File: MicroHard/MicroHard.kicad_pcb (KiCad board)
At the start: 4 copper layers, 0 parts

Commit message: Initial layout
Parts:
- added C1: 100n, Capacitor_SMD:C_1206_3216Metric_Pad1.33x1.80mm_HandSolder, F.Cu at (233.0, 79.0)
- added C10: 100n, Capacitor_SMD:C_1206_3216Metric_Pad1.33x1.80mm_HandSolder, F.Cu at (233.0, 85.5)
- added C11: 10u, Capacitor_SMD:C_1206_3216Metric_Pad1.33x1.80mm_HandSolder, F.Cu at (217.1, 80.0)
- added C12: 100n, Capacitor_SMD:C_1206_3216Metric_Pad1.33x1.80mm_HandSolder, F.Cu at (216.9, 85.5)
- added C13: 100n, Capacitor_SMD:C_1206_3216Metric_Pad1.33x1.80mm_HandSolder, F.Cu at (216.9, 90.5)
- added C14: 100n, Capacitor_SMD:C_1206_3216Metric_Pad1.33x1.80mm_HandSolder, F.Cu at (233.0, 90.5)
- added C15: 22u, Capacitor_SMD:C_1206_3216Metric_Pad1.33x1.80mm_HandSolder, F.Cu at (204.0, 84.6)
- added C16: 22u, Capacitor_SMD:C_1206_3216Metric_Pad1.33x1.80mm_HandSolder, F.Cu at (199.0, 84.5)
- added C17: 22u, Capacitor_SMD:C_1206_3216Metric_Pad1.33x1.80mm_HandSolder, F.Cu at (204.0, 91.0)
- added C18: 22u, Capacitor_SMD:C_1206_3216Metric_Pad1.33x1.80mm_HandSolder, F.Cu at (199.0, 91.0)
- added C19: 1u, Capacitor_SMD:C_1206_3216Metric_Pad1.33x1.80mm_HandSolder, F.Cu at (225.4, 94.2)
- added C2: 100u, Capacitor_SMD:C_1210_3225Metric_Pad1.33x2.70mm_HandSolder, F.Cu at (225.2, 66.5)
- added C20: 30p, Capacitor_SMD:C_0805_2012Metric_Pad1.18x1.45mm_HandSolder, F.Cu at (186.0, 136.8)
- added C21: 30p, Capacitor_SMD:C_0805_2012Metric_Pad1.18x1.45mm_HandSolder, F.Cu at (186.0, 133.8)
- added C22: 10u, Capacitor_SMD:C_1206_3216Metric_Pad1.33x1.80mm_HandSolder, F.Cu at (175.4, 121.7)
- added C23: 10n, Capacitor_SMD:C_1206_3216Metric_Pad1.33x1.80mm_HandSolder, F.Cu at (175.4, 118.3)
- added C24: 10n, Capacitor_SMD:C_1206_3216Metric_Pad1.33x1.80mm_HandSolder, F.Cu at (175.4, 115.0)
- added C25: 1u, Capacitor_SMD:C_1206_3216Metric_Pad1.33x1.80mm_HandSolder, F.Cu at (175.4, 111.7)
- added C26: 10u, Capacitor_SMD:C_1206_3216Metric_Pad1.33x1.80mm_HandSolder, F.Cu at (175.4, 108.3)
- added C27: 100n, Capacitor_SMD:C_1206_3216Metric_Pad1.33x1.80mm_HandSolder, F.Cu at (202.6, 108.3)
- added C28: 10u, Capacitor_SMD:C_1206_3216Metric_Pad1.33x1.80mm_HandSolder, F.Cu at (202.6, 112.3)
- added C29: 100n, Capacitor_SMD:C_1206_3216Metric_Pad1.33x1.80mm_HandSolder, F.Cu at (202.6, 115.7)
- added C3: 10u, Capacitor_SMD:C_1206_3216Metric_Pad1.33x1.80mm_HandSolder, F.Cu at (233.0, 71.2)
- added C30: 100n, Capacitor_SMD:C_1206_3216Metric_Pad1.33x1.80mm_HandSolder, F.Cu at (202.6, 119.0)
- added C31: 100n, Capacitor_SMD:C_1206_3216Metric_Pad1.33x1.80mm_HandSolder, F.Cu at (202.6, 122.3)
- added C32: 100u, Capacitor_SMD:C_1210_3225Metric_Pad1.33x2.70mm_HandSolder, F.Cu at (85.3, 141.9)
- added C33: 4.7u, Capacitor_SMD:C_0805_2012Metric_Pad1.18x1.45mm_HandSolder, F.Cu at (79.9, 141.3)
- added C34: 4.7u, Capacitor_SMD:C_0805_2012Metric_Pad1.18x1.45mm_HandSolder, F.Cu at (79.9, 144.3)
- added C35: 470n, Capacitor_SMD:C_0603_1608Metric_Pad1.08x0.95mm_HandSolder, F.Cu at (124.0, 129.8)
- added C36: 470n, Capacitor_SMD:C_0603_1608Metric_Pad1.08x0.95mm_HandSolder, F.Cu at (124.0, 132.3)
- added C37: 470n, Capacitor_SMD:C_0603_1608Metric_Pad1.08x0.95mm_HandSolder, F.Cu at (124.0, 134.8)
- added C38: 470n, Capacitor_SMD:C_0603_1608Metric_Pad1.08x0.95mm_HandSolder, F.Cu at (124.0, 137.3)
- added C39: 470n, Capacitor_SMD:C_0603_1608Metric_Pad1.08x0.95mm_HandSolder, F.Cu at (124.0, 139.8)
- added C4: 100n, Capacitor_SMD:C_1206_3216Metric_Pad1.33x1.80mm_HandSolder, F.Cu at (233.0, 75.0)
- added C40: 470n, Capacitor_SMD:C_0603_1608Metric_Pad1.08x0.95mm_HandSolder, F.Cu at (124.0, 142.3)
- added C41: 4.7u, Capacitor_SMD:C_0805_2012Metric_Pad1.18x1.45mm_HandSolder, F.Cu at (79.9, 147.3)
- added C42: 100u, Capacitor_SMD:C_1210_3225Metric_Pad1.33x2.70mm_HandSolder, F.Cu at (85.3, 146.2)
- added C43: 470n, Capacitor_SMD:C_0603_1608Metric_Pad1.08x0.95mm_HandSolder, F.Cu at (124.0, 144.8)
- added C44: 470n, Capacitor_SMD:C_0603_1608Metric_Pad1.08x0.95mm_HandSolder, F.Cu at (124.0, 147.3)
- added C45: 4.7u, Capacitor_SMD:C_0805_2012Metric_Pad1.18x1.45mm_HandSolder, F.Cu at (79.9, 150.3)
- added C46: 10n, Capacitor_SMD:C_1206_3216Metric_Pad1.33x1.80mm_HandSolder, F.Cu at (85.3, 150.0)
- added C47: 47u, Capacitor_SMD:C_1210_3225Metric_Pad1.33x2.70mm_HandSolder, F.Cu at (110.0, 155.8)
- added C48: 330u, Capacitor_Tantalum_SMD:CP_EIA-7343-31_Kemet-D_Pad2.25x2.55mm_HandSolder, F.Cu at (134.5, 145.3)
- added C49: 4.7u, Capacitor_SMD:C_0805_2012Metric_Pad1.18x1.45mm_HandSolder, F.Cu at (116.5, 147.3)
- added C5: 22u, Capacitor_SMD:C_1206_3216Metric_Pad1.33x1.80mm_HandSolder, F.Cu at (204.0, 78.9)
- added C50: 4.7u, Capacitor_SMD:C_0805_2012Metric_Pad1.18x1.45mm_HandSolder, F.Cu at (113.5, 147.3)
- added C51: 4.7u, Capacitor_SMD:C_0805_2012Metric_Pad1.18x1.45mm_HandSolder, F.Cu at (110.5, 147.3)
- added C52: 4.7u, Capacitor_SMD:C_0805_2012Metric_Pad1.18x1.45mm_HandSolder, F.Cu at (107.5, 147.3)
- added C53: 4.7u, Capacitor_SMD:C_0805_2012Metric_Pad1.18x1.45mm_HandSolder, F.Cu at (104.5, 147.3)
- added C54: 4.7u, Capacitor_SMD:C_0805_2012Metric_Pad1.18x1.45mm_HandSolder, F.Cu at (101.4, 147.3)
- added C55: 470n, Capacitor_SMD:C_0603_1608Metric_Pad1.08x0.95mm_HandSolder, F.Cu at (96.6, 139.6)
- added C56: 470n, Capacitor_SMD:C_0603_1608Metric_Pad1.08x0.95mm_HandSolder, F.Cu at (96.6, 137.1)
- added C57: 470n, Capacitor_SMD:C_0603_1608Metric_Pad1.08x0.95mm_HandSolder, F.Cu at (96.6, 134.5)
- added C58: 470n, Capacitor_SMD:C_0603_1608Metric_Pad1.08x0.95mm_HandSolder, F.Cu at (96.6, 132.0)
- added C59: 470n, Capacitor_SMD:C_0603_1608Metric_Pad1.08x0.95mm_HandSolder, F.Cu at (96.6, 129.5)
- added C6: 22u, Capacitor_SMD:C_1206_3216Metric_Pad1.33x1.80mm_HandSolder, F.Cu at (199.0, 79.0)
- added C60: 470n, Capacitor_SMD:C_0603_1608Metric_Pad1.08x0.95mm_HandSolder, F.Cu at (98.5, 121.2)
- added C61: 470n, Capacitor_SMD:C_0603_1608Metric_Pad1.08x0.95mm_HandSolder, F.Cu at (101.0, 121.2)
- added C62: 470n, Capacitor_SMD:C_0603_1608Metric_Pad1.08x0.95mm_HandSolder, F.Cu at (103.5, 121.2)
- added C63: 47u, Capacitor_SMD:C_1210_3225Metric_Pad1.33x2.70mm_HandSolder, F.Cu at (91.0, 121.3)
- added C64: 4.7u, Capacitor_SMD:C_0805_2012Metric_Pad1.18x1.45mm_HandSolder, F.Cu at (98.4, 147.3)
- added C65: 4.7u, Capacitor_SMD:C_0805_2012Metric_Pad1.18x1.45mm_HandSolder, F.Cu at (95.4, 147.3)
- added C66: 470n, Capacitor_SMD:C_0603_1608Metric_Pad1.08x0.95mm_HandSolder, F.Cu at (106.0, 121.2)
- added C67: 470n, Capacitor_SMD:C_0603_1608Metric_Pad1.08x0.95mm_HandSolder, F.Cu at (108.5, 121.2)
- added C68: 470n, Capacitor_SMD:C_0603_1608Metric_Pad1.08x0.95mm_HandSolder, F.Cu at (111.0, 121.3)
- added C69: 100u, Capacitor_SMD:C_1210_3225Metric_Pad1.33x2.70mm_HandSolder, F.Cu at (124.0, 121.8)
- added C7: 3.3n, Capacitor_SMD:C_1206_3216Metric_Pad1.33x1.80mm_HandSolder, F.Cu at (217.1, 75.5)
- added C70: 470n, Capacitor_SMD:C_0603_1608Metric_Pad1.08x0.95mm_HandSolder, F.Cu at (113.5, 121.3)
- added C71: 470n, Capacitor_SMD:C_0603_1608Metric_Pad1.08x0.95mm_HandSolder, F.Cu at (116.0, 121.3)
- added C72: 47u, Capacitor_SMD:C_1210_3225Metric_Pad1.33x2.70mm_HandSolder, F.Cu at (180.7, 86.3)
- added C73: 100n, Capacitor_SMD:C_1206_3216Metric_Pad1.33x1.80mm_HandSolder, F.Cu at (180.7, 89.8)
- added C74: 11p, Capacitor_SMD:C_0805_2012Metric_Pad1.18x1.45mm_HandSolder, F.Cu at (180.2, 92.8)
- added C75: 1u, Capacitor_SMD:C_1206_3216Metric_Pad1.33x1.80mm_HandSolder, F.Cu at (70.0, 98.8)
- added C76: 100n, Capacitor_SMD:C_1206_3216Metric_Pad1.33x1.80mm_HandSolder, F.Cu at (70.0, 95.5)
- added C77: 1u, Capacitor_SMD:C_1206_3216Metric_Pad1.33x1.80mm_HandSolder, F.Cu at (90.1, 99.4)
- added C78: 100n, Capacitor_SMD:C_1206_3216Metric_Pad1.33x1.80mm_HandSolder, F.Cu at (90.1, 96.0)
- added C79: 4p, Capacitor_SMD:C_1206_3216Metric_Pad1.33x1.80mm_HandSolder, F.Cu at (93.5, 59.8)
- added C8: 1u, Capacitor_SMD:C_1206_3216Metric_Pad1.33x1.80mm_HandSolder, F.Cu at (217.1, 71.0)
- added C80: 100n, Capacitor_SMD:C_1206_3216Metric_Pad1.33x1.80mm_HandSolder, F.Cu at (139.5, 110.3)
- added C81: 100n, Capacitor_SMD:C_1206_3216Metric_Pad1.33x1.80mm_HandSolder, F.Cu at (122.0, 100.3)
- added C9: 10u, Capacitor_SMD:C_1206_3216Metric_Pad1.33x1.80mm_HandSolder, F.Cu at (225.0, 80.0)
- added D1: LED, LED_SMD:LED_1206_3216Metric_Pad1.42x1.75mm_HandSolder, F.Cu at (216.9, 61.5)
- added D2: LED, LED_SMD:LED_1206_3216Metric_Pad1.42x1.75mm_HandSolder, F.Cu at (213.9, 116.6)
- added D3: LED, LED_SMD:LED_1206_3216Metric_Pad1.42x1.75mm_HandSolder, F.Cu at (219.4, 116.6)
- added D4: LED, LED_SMD:LED_1206_3216Metric_Pad1.42x1.75mm_HandSolder, F.Cu at (77.4, 132.2)
- added D5: LED, LED_SMD:LED_1206_3216Metric_Pad1.42x1.75mm_HandSolder, F.Cu at (77.4, 128.8)
- added D6: LED, LED_SMD:LED_1206_3216Metric_Pad1.42x1.75mm_HandSolder, F.Cu at (77.4, 125.4)
- added D7: LED, LED_SMD:LED_1206_3216Metric_Pad1.42x1.75mm_HandSolder, F.Cu at (77.4, 122.0)
- added FB1: FerriteBead, Resistor_SMD:R_1206_3216Metric_Pad1.30x1.75mm_HandSolder, F.Cu at (176.5, 136.0)
- added IC1: IS66WVO32M8DBLL-166BLI, MicroHard:BGA24C100P5X5_600X800X120, F.Cu at (113.0, 97.8)
- added J1: USB_B_Micro, Connector_USB:USB_Micro-B_Amphenol_10118194_Horizontal, F.Cu at (233.7, 62.5)
- added J2: Micro_SD_Card_Det2, Connector_Card:microSD_HC_Hirose_DM3AT-SF-PEJM5, F.Cu at (240.0, 114.8)
- added J3: GPIO_header, Connector_PinHeader_2.54mm:PinHeader_1x08_P2.54mm_Vertical, F.Cu at (166.5, 128.2)
- added J4: MCU_Debug, Connector_PinHeader_1.00mm:PinHeader_2x10_P1.00mm_Vertical, F.Cu at (207.9, 146.3)
- added J5: Controller Connector, Connector_PinHeader_2.54mm:PinHeader_1x07_P2.54mm_Vertical, F.Cu at (177.3, 146.8)
- added J6: FPGA_GPIO_header, Connector_JST:JST_XH_B8B-XH-AM_1x08_P2.50mm_Vertical, F.Cu at (161.0, 128.4)
- added J7: FPGA_DEBUG, MicroHard:MOLEX_87832-1420, F.Cu at (67.8, 126.3)
- added J8: L77HDE15SD1CH4FVGA, MicroHard:AMPHENOL_L77HDE15SD1CH4FVGA, F.Cu at (73.4, 57.9)
- added JP1: Jumper_2_Bridged, Connector_PinHeader_2.54mm:PinHeader_1x02_P2.54mm_Vertical, F.Cu at (191.8, 79.3)
- added JP2: Jumper_2_Bridged, Connector_PinHeader_2.54mm:PinHeader_1x02_P2.54mm_Vertical, F.Cu at (191.8, 84.0)
- added JP3: Jumper_2_Bridged, Connector_PinHeader_2.54mm:PinHeader_1x02_P2.54mm_Vertical, F.Cu at (191.8, 88.7)
- added L1: 1.5u, Inductor_SMD:L_1206_3216Metric_Pad1.42x1.75mm_HandSolder, F.Cu at (209.7, 79.0)
- added L2: 1.5u, Inductor_SMD:L_1206_3216Metric_Pad1.42x1.75mm_HandSolder, F.Cu at (209.7, 85.0)
- added L3: 2.2u, Inductor_SMD:L_1206_3216Metric_Pad1.42x1.75mm_HandSolder, F.Cu at (210.2, 91.0)
- added LED1: LTP-587HR, LTP-587HR:LTP-587HR_LTO, F.Cu at (103.1, 52.2)
- added LED2: LTP-587HR, LTP-587HR:LTP-587HR_LTO, F.Cu at (120.8, 52.2)
- added LED3: LTP-587HR, LTP-587HR:LTP-587HR_LTO, F.Cu at (138.5, 52.2)
- added LED4: LTP-587HR, LTP-587HR:LTP-587HR_LTO, F.Cu at (156.1, 52.2)
- added LED5: LTP-587HR, LTP-587HR:LTP-587HR_LTO, F.Cu at (173.8, 52.2)
- added LED6: LTP-587HR, LTP-587HR:LTP-587HR_LTO, F.Cu at (191.4, 52.2)
- added R1: 6.81k, Resistor_SMD:R_1206_3216Metric_Pad1.30x1.75mm_HandSolder, B.Cu at (210.3, 69.5)
- added R10: 22.1k, Resistor_SMD:R_1206_3216Metric_Pad1.30x1.75mm_HandSolder, B.Cu at (205.1, 86.0)
- added R11: 68, Resistor_SMD:R_1206_3216Metric_Pad1.30x1.75mm_HandSolder, F.Cu at (213.9, 110.6)
- added R12: 10k, Resistor_SMD:R_1206_3216Metric_Pad1.30x1.75mm_HandSolder, F.Cu at (221.5, 125.8)
- added R13: 68, Resistor_SMD:R_1206_3216Metric_Pad1.30x1.75mm_HandSolder, F.Cu at (219.4, 110.6)
- added R14: 10k, Resistor_SMD:R_1206_3216Metric_Pad1.30x1.75mm_HandSolder, F.Cu at (213.0, 125.8)
- added R15: 10k, Resistor_SMD:R_1206_3216Metric_Pad1.30x1.75mm_HandSolder, F.Cu at (140.0, 83.8)
- added R16: 200, Resistor_SMD:R_1206_3216Metric_Pad1.30x1.75mm_HandSolder, F.Cu at (68.5, 140.6)
- added R17: 4.7k, Resistor_SMD:R_1206_3216Metric_Pad1.30x1.75mm_HandSolder, F.Cu at (68.5, 143.8)
- added R18: 10k, Resistor_SMD:R_1206_3216Metric_Pad1.30x1.75mm_HandSolder, F.Cu at (68.5, 147.1)
- added R19: 10k, Resistor_SMD:R_1206_3216Metric_Pad1.30x1.75mm_HandSolder, F.Cu at (68.5, 150.4)
- added R2: 100k, Resistor_SMD:R_1206_3216Metric_Pad1.30x1.75mm_HandSolder, B.Cu at (210.2, 74.9)
- added R20: 4.7k, Resistor_SMD:R_1206_3216Metric_Pad1.30x1.75mm_HandSolder, F.Cu at (132.5, 83.9)
- added R21: 100, Resistor_SMD:R_1206_3216Metric_Pad1.30x1.75mm_HandSolder, F.Cu at (83.4, 132.1)
- added R22: 330, Resistor_SMD:R_1206_3216Metric_Pad1.30x1.75mm_HandSolder, F.Cu at (83.4, 128.8)
- added R23: 330, Resistor_SMD:R_1206_3216Metric_Pad1.30x1.75mm_HandSolder, F.Cu at (83.4, 125.5)
- added R24: 330, Resistor_SMD:R_1206_3216Metric_Pad1.30x1.75mm_HandSolder, F.Cu at (83.4, 122.3)
- added R25: 4.7k, Resistor_SMD:R_1206_3216Metric_Pad1.30x1.75mm_HandSolder, F.Cu at (154.2, 85.8)
- added R26: 4.7k, Resistor_SMD:R_1206_3216Metric_Pad1.30x1.75mm_HandSolder, F.Cu at (154.2, 88.8)
- added R27: 112k, Resistor_SMD:R_1206_3216Metric_Pad1.30x1.75mm_HandSolder, F.Cu at (154.2, 92.3)
- added R28: 100k, Resistor_SMD:R_1206_3216Metric_Pad1.30x1.75mm_HandSolder, B.Cu at (69.4, 109.8)
- added R29: 100k, Resistor_SMD:R_1206_3216Metric_Pad1.30x1.75mm_HandSolder, B.Cu at (72.7, 109.8)
- added R3: 22.1k, Resistor_SMD:R_1206_3216Metric_Pad1.30x1.75mm_HandSolder, B.Cu at (210.4, 65.0)
- added R30: 100k, Resistor_SMD:R_1206_3216Metric_Pad1.30x1.75mm_HandSolder, B.Cu at (76.0, 109.8)
- added R31: 100k, Resistor_SMD:R_1206_3216Metric_Pad1.30x1.75mm_HandSolder, B.Cu at (79.3, 109.8)
- added R32: 536, Resistor_SMD:R_1206_3216Metric_Pad1.30x1.75mm_HandSolder, F.Cu at (62.0, 73.4)
- added R33: 270, Resistor_SMD:R_1206_3216Metric_Pad1.30x1.75mm_HandSolder, F.Cu at (65.0, 70.4)
- added R34: 536, Resistor_SMD:R_1206_3216Metric_Pad1.30x1.75mm_HandSolder, F.Cu at (68.0, 73.4)
- added R35: 536, Resistor_SMD:R_1206_3216Metric_Pad1.30x1.75mm_HandSolder, F.Cu at (91.0, 85.3)
- added R36: 100k, Resistor_SMD:R_1206_3216Metric_Pad1.30x1.75mm_HandSolder, B.Cu at (92.1, 109.8)
- added R37: 100k, Resistor_SMD:R_1206_3216Metric_Pad1.30x1.75mm_HandSolder, B.Cu at (88.8, 109.8)
- added R38: 100k, Resistor_SMD:R_1206_3216Metric_Pad1.30x1.75mm_HandSolder, B.Cu at (85.5, 109.8)
- added R39: 100k, Resistor_SMD:R_1206_3216Metric_Pad1.30x1.75mm_HandSolder, B.Cu at (82.2, 109.8)
- added R4: 1, Resistor_SMD:R_1206_3216Metric_Pad1.30x1.75mm_HandSolder, F.Cu at (176.4, 140.5)
- added R40: 270, Resistor_SMD:R_1206_3216Metric_Pad1.30x1.75mm_HandSolder, F.Cu at (71.0, 70.4)
- added R41: 270, Resistor_SMD:R_1206_3216Metric_Pad1.30x1.75mm_HandSolder, F.Cu at (94.5, 82.3)
- added R42: 536, Resistor_SMD:R_1206_3216Metric_Pad1.30x1.75mm_HandSolder, F.Cu at (74.0, 73.4)
- added R43: 536, Resistor_SMD:R_1206_3216Metric_Pad1.30x1.75mm_HandSolder, F.Cu at (98.0, 85.3)
- added R44: 536, Resistor_SMD:R_1206_3216Metric_Pad1.30x1.75mm_HandSolder, F.Cu at (63.9, 85.3)
- added R45: 270, Resistor_SMD:R_1206_3216Metric_Pad1.30x1.75mm_HandSolder, F.Cu at (77.0, 70.4)
- added R46: 270, Resistor_SMD:R_1206_3216Metric_Pad1.30x1.75mm_HandSolder, F.Cu at (101.5, 82.3)
- added R47: 270, Resistor_SMD:R_1206_3216Metric_Pad1.30x1.75mm_HandSolder, F.Cu at (67.0, 81.3)
- added R48: 536, Resistor_SMD:R_1206_3216Metric_Pad1.30x1.75mm_HandSolder, F.Cu at (80.5, 73.4)
- added R49: 536, Resistor_SMD:R_1206_3216Metric_Pad1.30x1.75mm_HandSolder, F.Cu at (104.5, 85.3)
- added R5: 30.1k, Resistor_SMD:R_1206_3216Metric_Pad1.30x1.75mm_HandSolder, B.Cu at (198.6, 81.5)
- added R50: 536, Resistor_SMD:R_1206_3216Metric_Pad1.30x1.75mm_HandSolder, F.Cu at (70.5, 85.3)
- added R51: 536, Resistor_SMD:R_1206_3216Metric_Pad1.30x1.75mm_HandSolder, F.Cu at (83.5, 70.4)
- added R52: 270, Resistor_SMD:R_1206_3216Metric_Pad1.30x1.75mm_HandSolder, F.Cu at (107.5, 82.3)
- added R53: 270, Resistor_SMD:R_1206_3216Metric_Pad1.30x1.75mm_HandSolder, F.Cu at (74.0, 81.8)
- added R54: 536, Resistor_SMD:R_1206_3216Metric_Pad1.30x1.75mm_HandSolder, F.Cu at (110.5, 85.8)
- added R55: 536, Resistor_SMD:R_1206_3216Metric_Pad1.30x1.75mm_HandSolder, F.Cu at (77.5, 85.3)
- added R56: 536, Resistor_SMD:R_1206_3216Metric_Pad1.30x1.75mm_HandSolder, F.Cu at (113.5, 82.3)
- added R57: 270, Resistor_SMD:R_1206_3216Metric_Pad1.30x1.75mm_HandSolder, F.Cu at (81.0, 81.8)
- added R58: 536, Resistor_SMD:R_1206_3216Metric_Pad1.30x1.75mm_HandSolder, F.Cu at (84.5, 85.3)
- added R59: 1MEG, Resistor_SMD:R_1206_3216Metric_Pad1.30x1.75mm_HandSolder, F.Cu at (93.4, 63.8)
- added R6: 73.2k, Resistor_SMD:R_1206_3216Metric_Pad1.30x1.75mm_HandSolder, B.Cu at (198.6, 86.0)
- added R60: 536, Resistor_SMD:R_1206_3216Metric_Pad1.30x1.75mm_HandSolder, F.Cu at (87.5, 81.8)
- added R61: 100k, Resistor_SMD:R_1206_3216Metric_Pad1.30x1.75mm_HandSolder, B.Cu at (96.8, 109.8)
- added R62: 100k, Resistor_SMD:R_1206_3216Metric_Pad1.30x1.75mm_HandSolder, B.Cu at (100.1, 109.8)
- added R63: 100k, Resistor_SMD:R_1206_3216Metric_Pad1.30x1.75mm_HandSolder, B.Cu at (104.5, 109.8)
- added R64: 100k, Resistor_SMD:R_1206_3216Metric_Pad1.30x1.75mm_HandSolder, B.Cu at (107.8, 109.8)
- added R65: 100, Resistor_SMD:R_1206_3216Metric_Pad1.30x1.75mm_HandSolder, F.Cu at (93.4, 68.8)
- added R66: 100, Resistor_SMD:R_1206_3216Metric_Pad1.30x1.75mm_HandSolder, F.Cu at (93.4, 72.1)
- added R67: 100k, Resistor_SMD:R_1206_3216Metric_Pad1.30x1.75mm_HandSolder, B.Cu at (114.5, 109.8)
- added R68: 100k, Resistor_SMD:R_1206_3216Metric_Pad1.30x1.75mm_HandSolder, B.Cu at (111.0, 109.8)
- added R69: 4.7k, Resistor_SMD:R_1206_3216Metric_Pad1.30x1.75mm_HandSolder, B.Cu at (139.4, 106.3)
- added R7: 100k, Resistor_SMD:R_1206_3216Metric_Pad1.30x1.75mm_HandSolder, B.Cu at (225.0, 94.2)
- added R70: 2.4k, Resistor_SMD:R_1206_3216Metric_Pad1.30x1.75mm_HandSolder, B.Cu at (141.9, 119.3)
- added R71: 4.7k, Resistor_SMD:R_1206_3216Metric_Pad1.30x1.75mm_HandSolder, F.Cu at (160.5, 111.3)
- added R72: 2.4k, Resistor_SMD:R_1206_3216Metric_Pad1.30x1.75mm_HandSolder, F.Cu at (122.0, 93.5)
- added R73: 2.4k, Resistor_SMD:R_1206_3216Metric_Pad1.30x1.75mm_HandSolder, F.Cu at (122.0, 96.8)
- added R8: 68, Resistor_SMD:R_1206_3216Metric_Pad1.30x1.75mm_HandSolder, F.Cu at (216.9, 66.5)
- added R9: 22.1k, Resistor_SMD:R_1206_3216Metric_Pad1.30x1.75mm_HandSolder, B.Cu at (205.1, 81.5)
- added SW1: KMR221NGLFS, KMR221NG:KMR221_CNK, F.Cu at (221.6, 132.1)
- added SW2: KMR221NGLFS, KMR221NG:KMR221_CNK, F.Cu at (212.9, 132.1)
- added SW3: KMR221NGLFS, KMR221NG:KMR221_CNK, F.Cu at (140.0, 91.8)
- added SW4: KMR221NGLFS, KMR221NG:KMR221_CNK, F.Cu at (132.5, 91.8)
- added TP1: TestPoint, TestPoint:TestPoint_Pad_D2.0mm, F.Cu at (129.5, 106.3)
- added TP2: TestPoint, TestPoint:TestPoint_Pad_D2.0mm, F.Cu at (122.5, 157.3)
- added TP3: TestPoint, TestPoint:TestPoint_Pad_D2.0mm, F.Cu at (127.0, 157.3)
- added U1: TPS54325, TPS54325PWP:PWP14_2P31X2P46, F.Cu at (225.0, 73.0)
- added U2: TPS54294, TPS54294PWP:PWP16_2P31X2P46, F.Cu at (225.2, 88.1)
- added U3: EFM32GG842F1024, EFM32GG842F1024:QFP64_10X10, F.Cu at (189.0, 115.5)
- added U4: XC7A100T-FTG256, MicroHard:BGA256C100P16X16_1700X1700X155, F.Cu at (109.5, 133.8)
- added U5: MAX6955 Display Driver, MAX6955:21-0040_A36&plus_2_MXM, F.Cu at (167.5, 89.3)
- added U6: SN74ALVC245PWR, footprints:PW20, F.Cu at (77.5, 97.3)
- added U7: SN74ALVC245PWR, footprints:PW20, F.Cu at (98.0, 97.3)
- added U8: MT25QL256ABA8ESF-0SIT, MicroHard:SOIC127P1032X265-16N, F.Cu at (151.0, 111.3)
- added Y1: 48MHz, Crystal:Crystal_SMD_3225-4Pin_3.2x2.5mm_HandSoldering, F.Cu at (193.0, 135.3)
- added Y2: CB3-3C-20M000000, MicroHard:OSC_CB3-3C-20M000000, F.Cu at (134.5, 136.3)

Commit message: VGA and Display layout
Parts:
- added R74: 12k, Resistor_SMD:R_1206_3216Metric_Pad1.30x1.75mm_HandSolder, B.Cu at (97.5, 51.5)
- C35, C36, C37, C38, C39, C40, C43, C44, C47, C49, C50, C51, C52, C53, C54, C55, C56, C57, C58, C59, C60, C61, C62, C64, C65, C66, C67, C68, C70, C71, C74, R35, R41, R43, R46, R49, R52, R54, R56: moved to B.Cu
- J6: footprint Connector_JST:JST_XH_B8B-XH-AM_1x08_P2.50mm_Vertical -> Connector_PinHeader_2.54mm:PinHeader_1x08_P2.54mm_Vertical
- R27: value 112k -> 100k; moved to B.Cu
- R8: value 68 -> 330
- moved R27 72.7 mm to (97.5, 47.0), turned to 180 degrees
- moved C74 72.1 mm to (119.8, 53.5)
- moved U5 71.9 mm to (109.0, 47.5)
- moved R26 71.9 mm to (97.5, 44.8)
- moved C72 69.9 mm to (121.2, 49.5)
- moved C73 69.6 mm to (121.2, 53.5)
- moved R56 69.0 mm to (51.8, 51.4)
- moved R25 67.5 mm to (97.5, 49.2)
- moved R54 63.9 mm to (54.8, 54.5)
- moved R52 58.5 mm to (57.8, 51.4)
- moved R49 53.4 mm to (60.8, 54.5)
- moved R46 48.7 mm to (63.8, 51.4)
- moved C48 48.5 mm to (86.0, 144.5)
- moved R51 44.9 mm to (42.7, 51.4)
- moved R43 43.8 mm to (66.8, 54.5)
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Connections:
- R27 pad 2: GND -> Net-(R27-Pad2)
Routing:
- net DD_O3: track 0.00 -> 188.2 mm, vias 0 -> 2
- net DD_O6: track 0.00 -> 167.8 mm
- net DD_O2: track 0.00 -> 141.1 mm, vias 0 -> 1
- net DD_O18: track 0.00 -> 139.4 mm, vias 0 -> 1
- net DD_O8: track 0.00 -> 131.7 mm
- net DD_O16: track 0.00 -> 129.6 mm, vias 0 -> 1
- net DD_O7: track 0.00 -> 129.3 mm
- net DD_O14: track 0.00 -> 126.9 mm, vias 0 -> 1
- net DD_O11: track 0.00 -> 125.9 mm
- net DD_O1: track 0.00 -> 125.8 mm, vias 0 -> 1
- net DD_O0: track 0.00 -> 125.4 mm, vias 0 -> 1
- net DD_O10: track 0.00 -> 124.3 mm
- net DD_O15: track 0.00 -> 123.9 mm, vias 0 -> 1
- net DD_O4: track 0.00 -> 122.7 mm, vias 0 -> 1
- net DD_O17: track 0.00 -> 117.9 mm, vias 0 -> 1
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- added copper zone on In2.Cu, net +3.3V
- added copper zone on In1.Cu, net GND
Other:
- board outline added: 222 x 144.5 mm

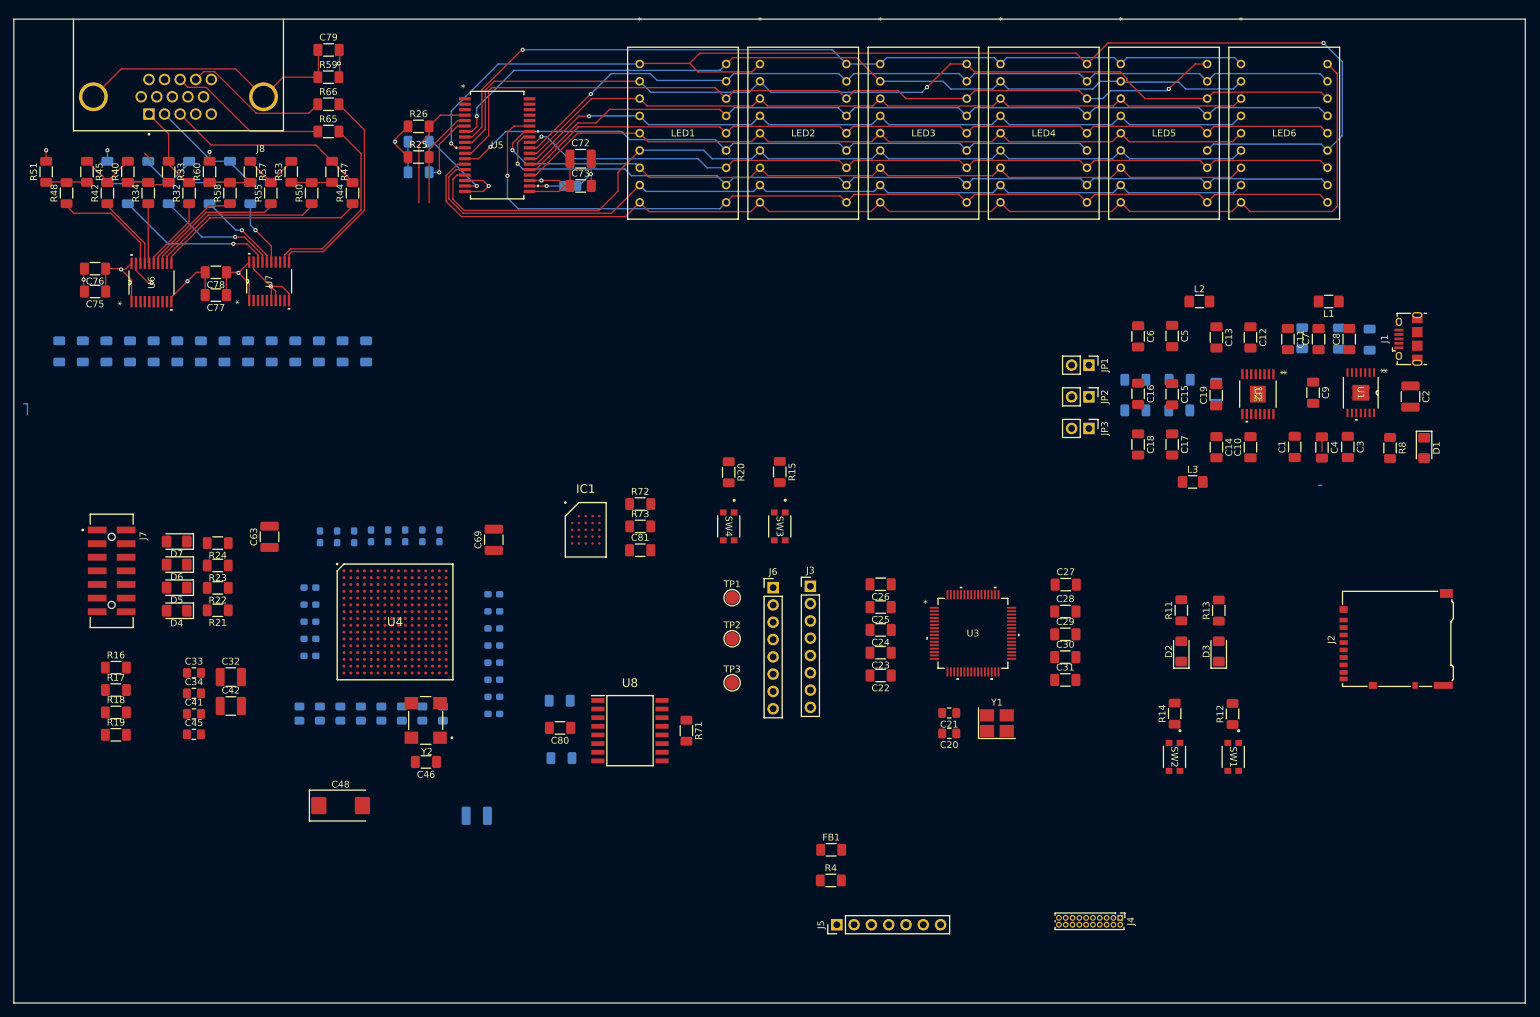
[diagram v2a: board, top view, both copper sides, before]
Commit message: power plane
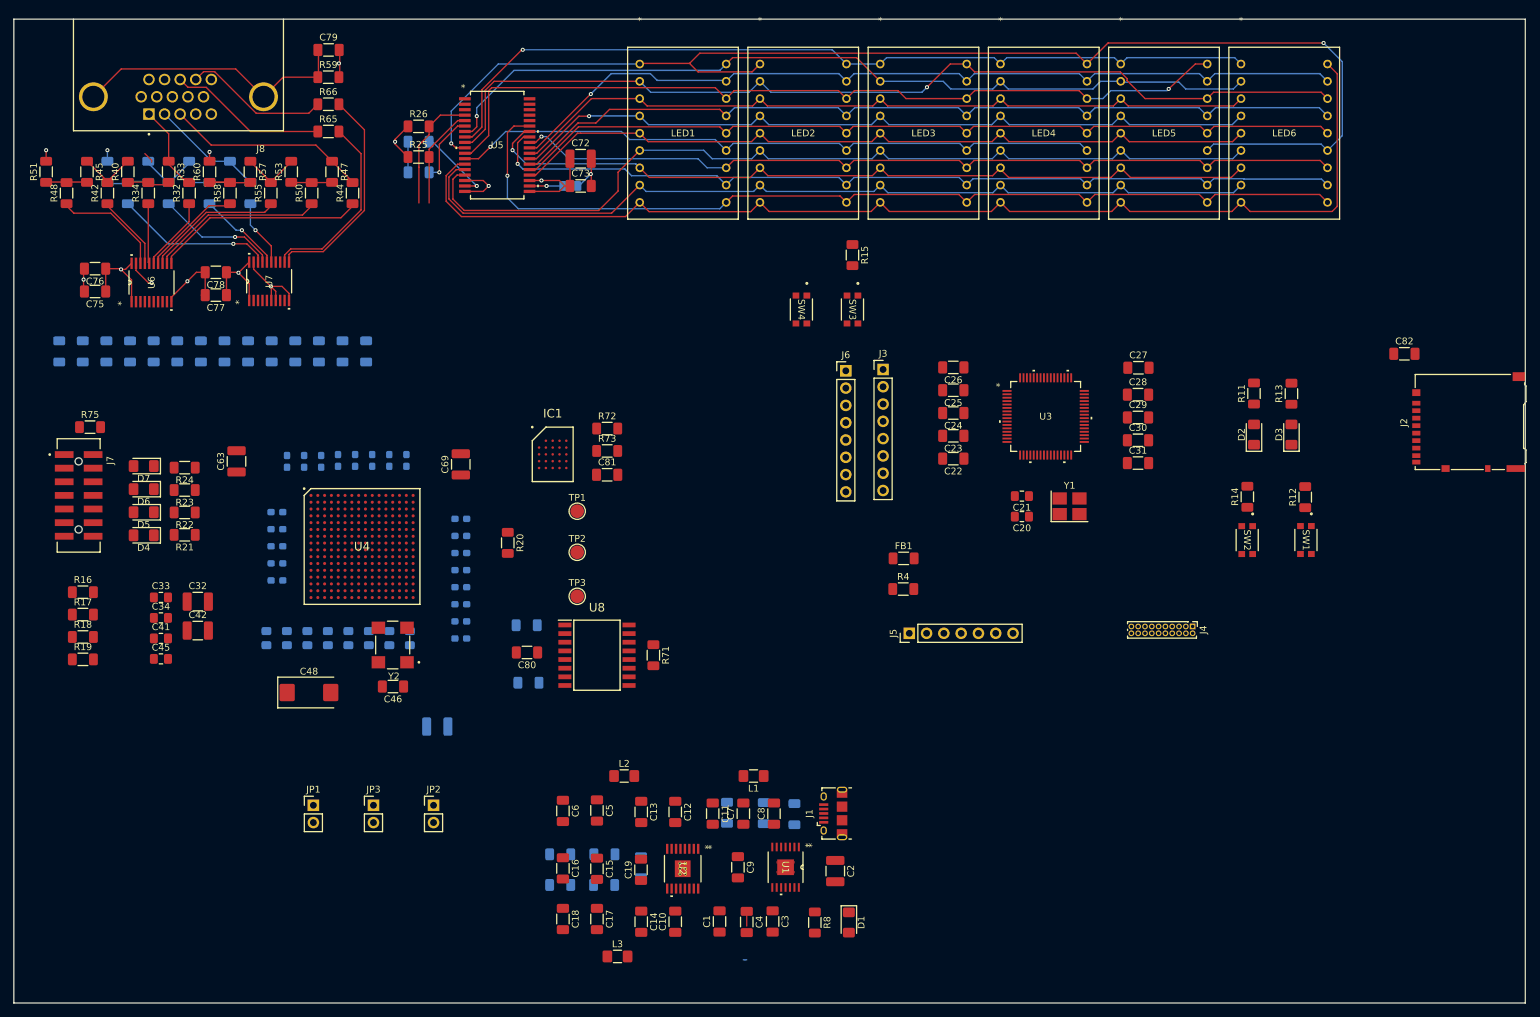
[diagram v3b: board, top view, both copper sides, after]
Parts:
- added C82: 100n, Capacitor_SMD:C_1206_3216Metric_Pad1.33x1.80mm_HandSolder, F.Cu at (242.2, 78.2)
- added R75: 10k, Resistor_SMD:R_1206_3216Metric_Pad1.30x1.75mm_HandSolder, F.Cu at (49.2, 88.9)
- moved JP1 131.0 mm to (82.0, 144.5), turned to 0 degrees
- moved JP3 118.8 mm to (90.8, 144.5), turned to 0 degrees
- moved JP2 113.4 mm to (99.7, 144.5), turned to 0 degrees
- moved D1 109.5 mm to (160.7, 161.7)
- moved R1 109.5 mm to (148.2, 145.6)
- moved R8 109.5 mm to (155.7, 161.7)
- moved U2 109.5 mm to (136.2, 153.8)
- moved C1 109.5 mm to (141.7, 161.5)
- moved C10 109.5 mm to (135.2, 161.6)
- moved C11 109.5 mm to (140.7, 145.7)
- moved C12 109.5 mm to (135.2, 145.4)
- moved C13 109.5 mm to (130.2, 145.4)
- moved C14 109.5 mm to (130.2, 161.6)
- moved C15 109.5 mm to (123.7, 153.8)
- moved C16 109.5 mm to (118.7, 153.7)
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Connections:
- U4 pad A6: unconnected-(U4B-VCCO_35-PadA6) -> GND
- U4 pad B3: unconnected-(U4B-VCCO_35-PadB3) -> GND
- U4 pad D7: unconnected-(U4B-VCCO_35-PadD7) -> GND
- U4 pad E4: unconnected-(U4B-VCCO_35-PadE4) -> GND
- U4 pad F1: unconnected-(U4B-VCCO_35-PadF1) -> GND
- U4 pad J2: unconnected-(U4B-VCCO_35-PadJ2) -> GND
- U4 pad M3: unconnected-(U4B-VCCO_34-PadM3) -> GND
- U4 pad R4: unconnected-(U4B-VCCO_34-PadR4) -> GND
- U4 pad T1: unconnected-(U4B-VCCO_34-PadT1) -> GND
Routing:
- net (no net): track 4.26 -> 2.16 mm
- added copper zone on In2.Cu, net +1V0
- added copper zone on In2.Cu, net +1V8

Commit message: Power supply layout
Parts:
- added R76: 1, Resistor_SMD:R_1206_3216Metric_Pad1.30x1.75mm_HandSolder, F.Cu at (88.5, 138.0)
- added R77: 47k, Resistor_SMD:R_1206_3216Metric_Pad1.30x1.75mm_HandSolder, F.Cu at (246.2, 104.7)
- added R78: 47k, Resistor_SMD:R_1206_3216Metric_Pad1.30x1.75mm_HandSolder, F.Cu at (246.2, 108.0)
- C13, C14: moved to B.Cu
- R1, R10, R3, R5, R6, R9: moved to F.Cu
- moved J1 118.9 mm to (40.8, 128.2), turned to -90 degrees
- moved D1 118.7 mm to (42.0, 157.3), turned to 90 degrees
- moved C2 116.0 mm to (46.2, 125.2), turned to 90 degrees
- moved R8 109.7 mm to (46.0, 157.3), turned to 90 degrees
- moved C3 100.5 mm to (53.0, 133.2)
- moved C8 98.5 mm to (55.0, 118.5), turned to 180 degrees
- moved U1 97.3 mm to (58.2, 125.2)
- moved C4 93.8 mm to (56.2, 133.2)
- moved C9 93.7 mm to (51.5, 141.2)
- moved C11 90.2 mm to (51.2, 157.3), turned to 90 degrees
- moved R2 88.3 mm to (58.5, 119.2), turned to 180 degrees
- moved C7 87.9 mm to (61.6, 118.5), turned to 0 degrees
- moved C1 87.1 mm to (62.6, 125.0)
- moved FB1 86.8 mm to (88.5, 141.5)
- moved R4 86.4 mm to (88.5, 145.0), turned to 180 degrees
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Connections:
- C1 pad 1: Net-(U1-SW1) -> Net-(U1-VCC)
- C1 pad 2: Net-(U1-VBST) -> Net-(U1-VO)
- C7 pad 1: Net-(U1-SS) -> Net-(U1-VREG5)
- C8 pad 1: Net-(U1-VREG5) -> Net-(U1-SS)
- C82 pad 1: +3.3VA -> +3.3V
- FB1 pad 1: +3.3V -> Net-(JP3-B)
- J2 pad 1: unconnected-(J2-DAT2-Pad1) -> Net-(J2-DAT2)
- J2 pad 4: +3.3VA -> +3.3V
- J2 pad 8: unconnected-(J2-DAT1-Pad8) -> Net-(J2-DAT1)
- JP3 pad 2: +3.3V -> Net-(JP3-B)
- L1 pad 1: Net-(U1-SW1) -> Net-(U1-VCC)
- R1 pad 2: Net-(U1-VFB) -> Net-(U1-PG)
- R2 pad 2: Net-(U1-VREG5) -> Net-(U1-SS)
- R3 pad 1: Net-(U1-VFB) -> Net-(U1-PG)
- U1 pad 1: Net-(JP1-A) -> Net-(U1-VO)
- U1 pad 10: Net-(U1-SW1) -> /Power Supply/POWER_IN
- U1 pad 11: Net-(U1-SW1) -> /Power Supply/POWER_IN
- U1 pad 12: Net-(U1-VBST) -> Net-(JP1-A)
- U1 pad 13: /Power Supply/POWER_IN -> Net-(U1-VCC)
- U1 pad 14: /Power Supply/POWER_IN -> Net-(U1-VCC)
- U1 pad 2: Net-(U1-VFB) -> /Power Supply/EN1.8V
- U1 pad 6: /Power Supply/EN1.8V -> Net-(U1-PG)
- U1 pad 7: /Power Supply/POWER_IN -> GND
- U1 pad 8: GND -> /Power Supply/POWER_IN
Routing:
- net /Power Supply/POWER_IN: track 2.21 -> 78.2 mm
- net /Power Supply/EN1.8V: track 0.00 -> 45.4 mm, vias 0 -> 2
- net GND: track 69.0 -> 114.2 mm, vias 11 -> 33
- net Net-(U1-PG): track 0.00 -> 33.5 mm, vias 0 -> 2
- net Net-(JP1-A): track 0.00 -> 27.2 mm
- net Net-(U2-VFB2): track 0.00 -> 22.2 mm
- net Net-(U2-VFB1): track 0.00 -> 21.9 mm
- net /Power Supply/EN3.3V: track 0.00 -> 21.2 mm, vias 0 -> 2
- net Net-(JP2-A): track 0.00 -> 19.2 mm
- net Net-(JP3-A): track 0.00 -> 17.2 mm
- net Net-(U2-SW2): track 0.00 -> 13.5 mm, vias 0 -> 1
- net Net-(U2-SW1): track 0.00 -> 12.7 mm, vias 0 -> 1
- net Net-(U1-VCC): track 0.00 -> 9.86 mm
- net Net-(FB1-Pad2): track 0.00 -> 7.00 mm
- net Net-(U2-VREG5): track 0.00 -> 6.23 mm, vias 0 -> 1
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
